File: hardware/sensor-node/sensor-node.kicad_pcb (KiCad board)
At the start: 2 copper layers, 57 x 57 mm, 52 parts, among them J1 CONUFL001-SMD-T, J2 Conn_ARM_JTAG_SWD_10, Q1 PMV250EPEA, U1 AAT1217, U2 TPS27081A, U3 SHT31-DIS, U4 24LC32, U5 MLX90614, U6 ADG633YCP, U7 TSV911RILT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

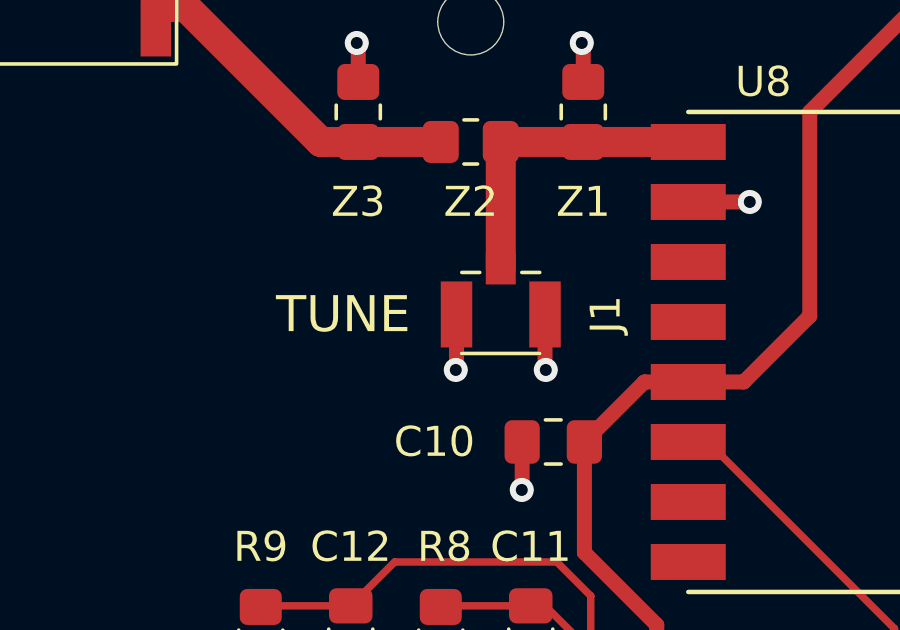
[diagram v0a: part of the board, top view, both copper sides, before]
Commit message: Add design resources and logo to PCB silkscreen
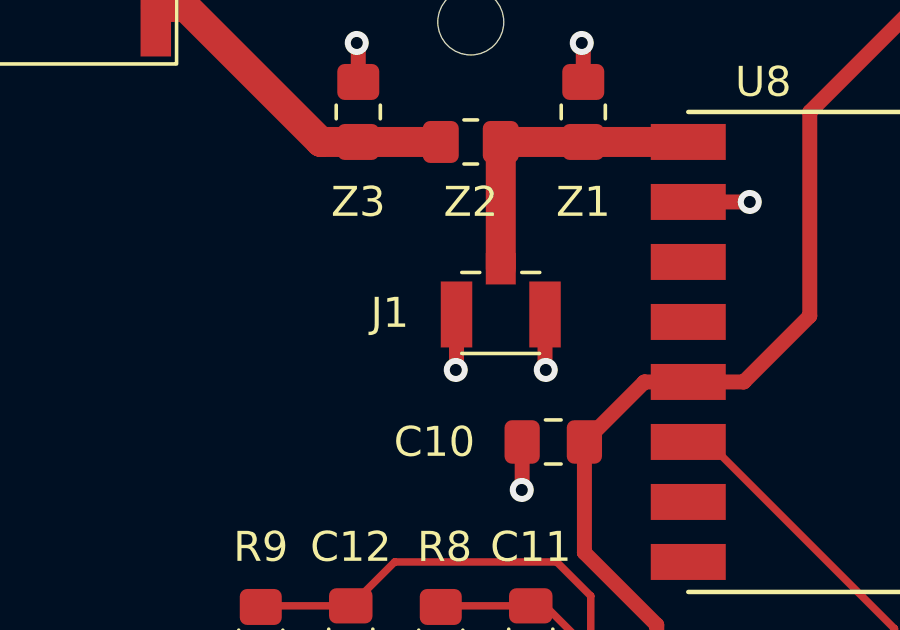
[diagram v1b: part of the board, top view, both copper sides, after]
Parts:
- added G***: LOGO, my-footprints-library:ProsperIIIKlimaMonitorLogo, B.Cu at (110.0, 46.7)
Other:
- board text added: "Sensor Node Rev. 1"
- board text removed: "FLASH"
- board text removed: "TUNE"

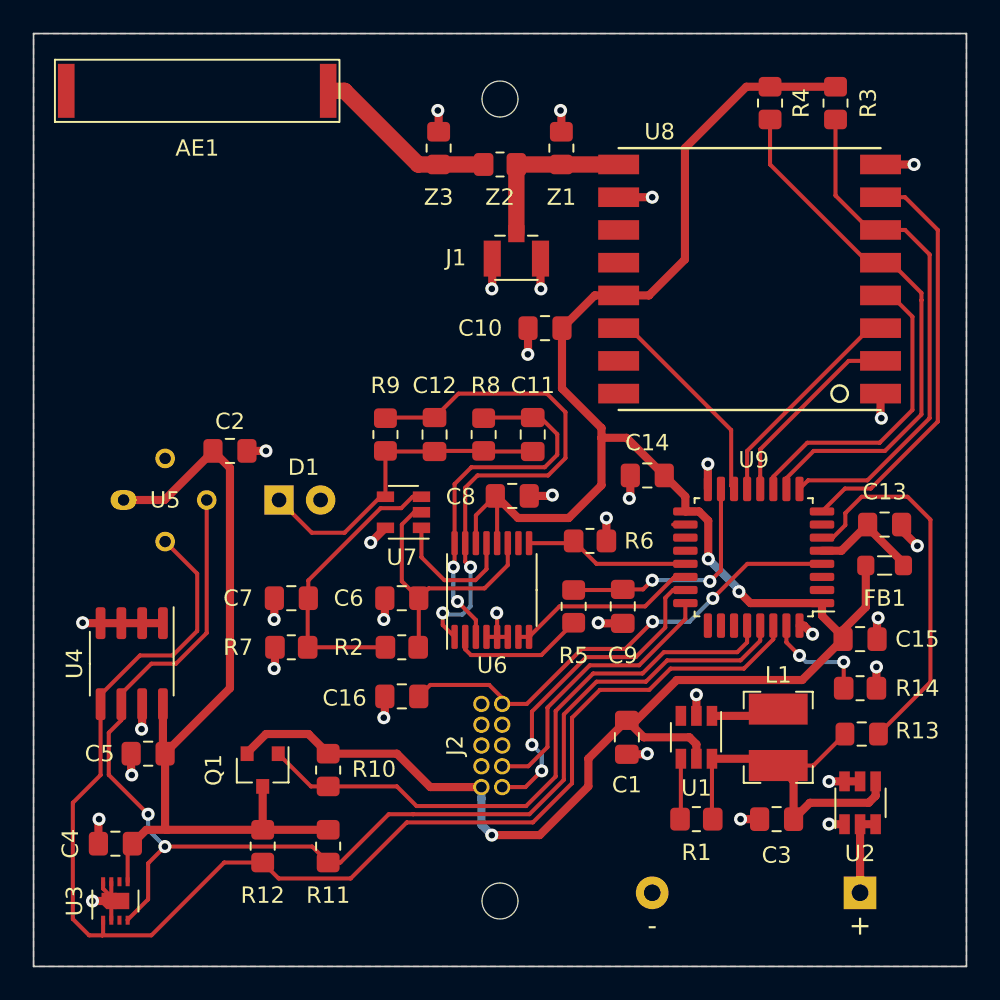
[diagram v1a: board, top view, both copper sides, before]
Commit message: Add picket fence vias
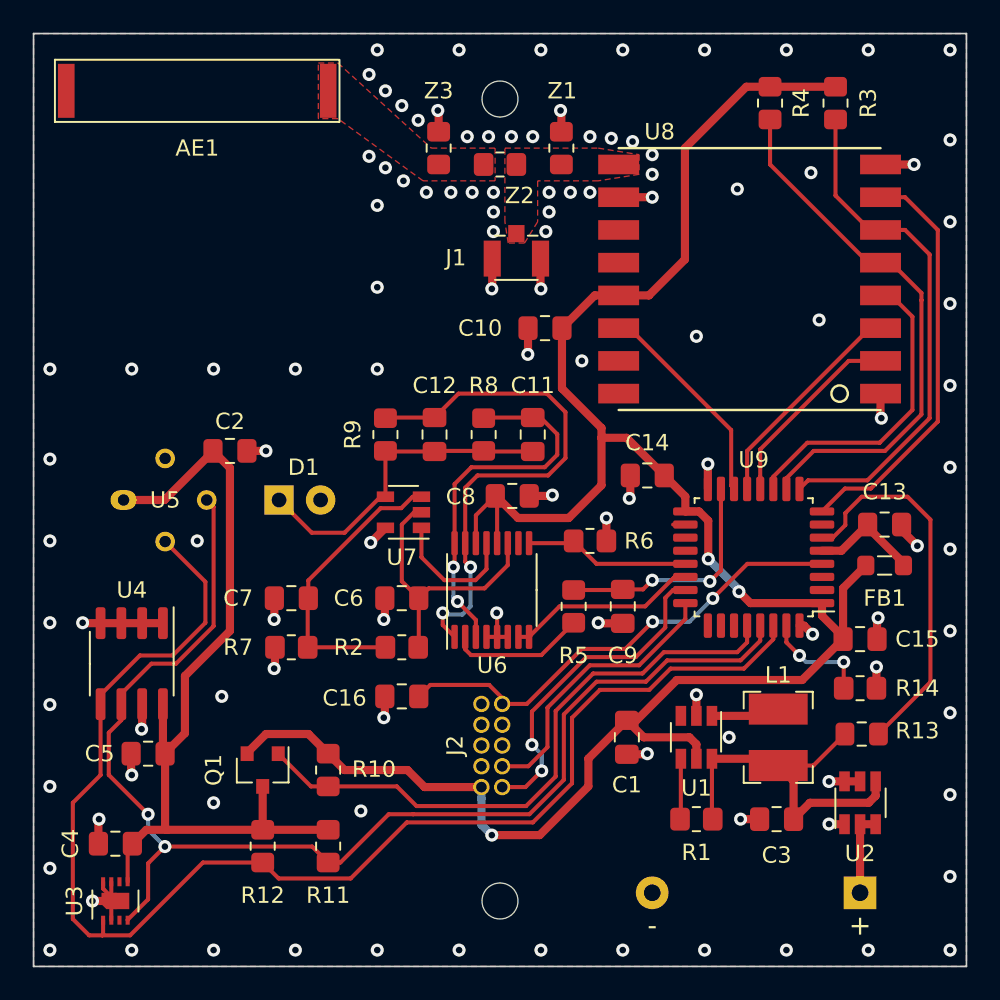
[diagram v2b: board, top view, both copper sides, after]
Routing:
- net Net-(AE1-Pad1): track 11.4 -> 0.00 mm
- net Net-(J1-Pad1): track 10.5 -> 0.00 mm
- net GND: vias 34 -> 114
- added copper zone on F.Cu, net GND
- added copper zone on F.Cu, net Net-(AE1-Pad1)
- added copper zone on F.Cu, net Net-(J1-Pad1)
- removed copper zone on F.Cu, net (none)

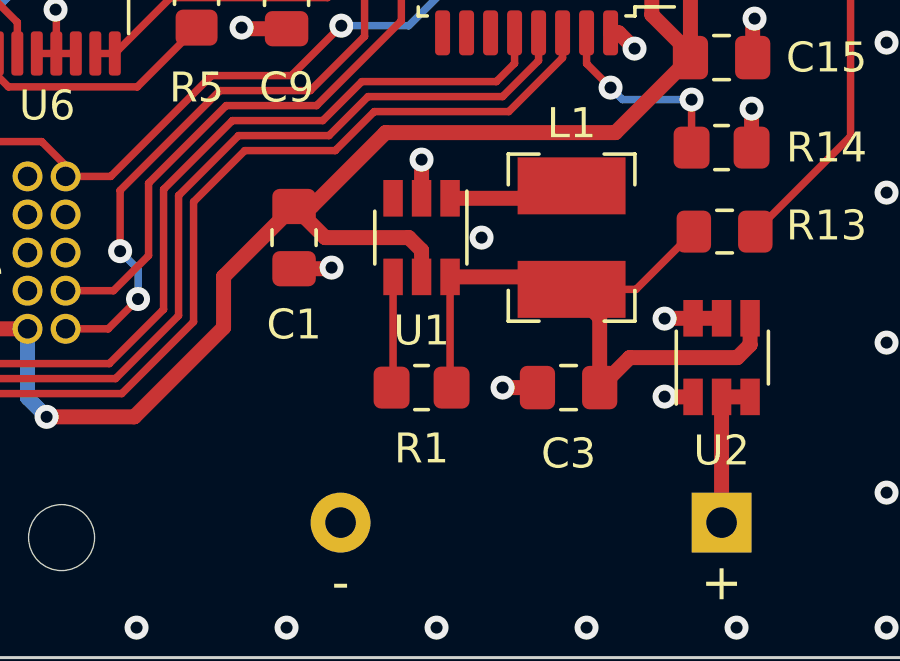
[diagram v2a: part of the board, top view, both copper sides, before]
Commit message: Switch to available boost converter
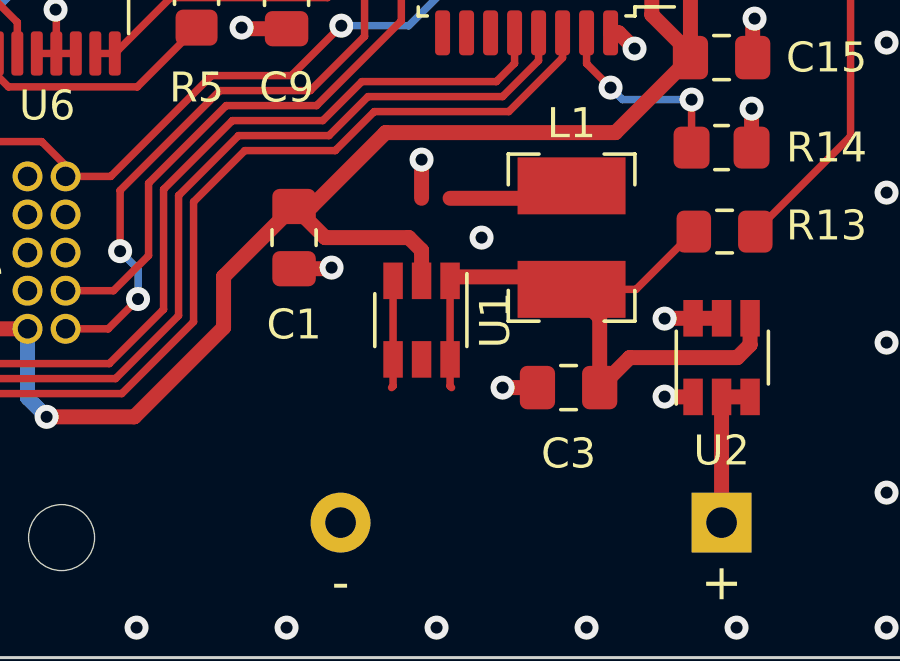
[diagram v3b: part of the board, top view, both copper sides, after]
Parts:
- removed G***: LOGO, my-footprints-library:ProsperIIIKlimaMonitorLogo
- removed R1: 1M, Resistor_SMD:R_0805_2012Metric_Pad1.20x1.40mm_HandSolder
- C1, C3: value 4.7uF -> 10uF
- U1: value AAT1217 -> TLV61225
- moved U1 2.75 mm to (140.5, 88.8)
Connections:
- U1 pad 1: Net-(L1-Pad1) -> VIN_SENSE
- U1 pad 2: GND -> +3V3
- U1 pad 3: Net-(U1-Pad3) -> GND
- U1 pad 4: Net-(R1-Pad2) -> +3V3
- U1 pad 5: +3V3 -> Net-(L1-Pad1)

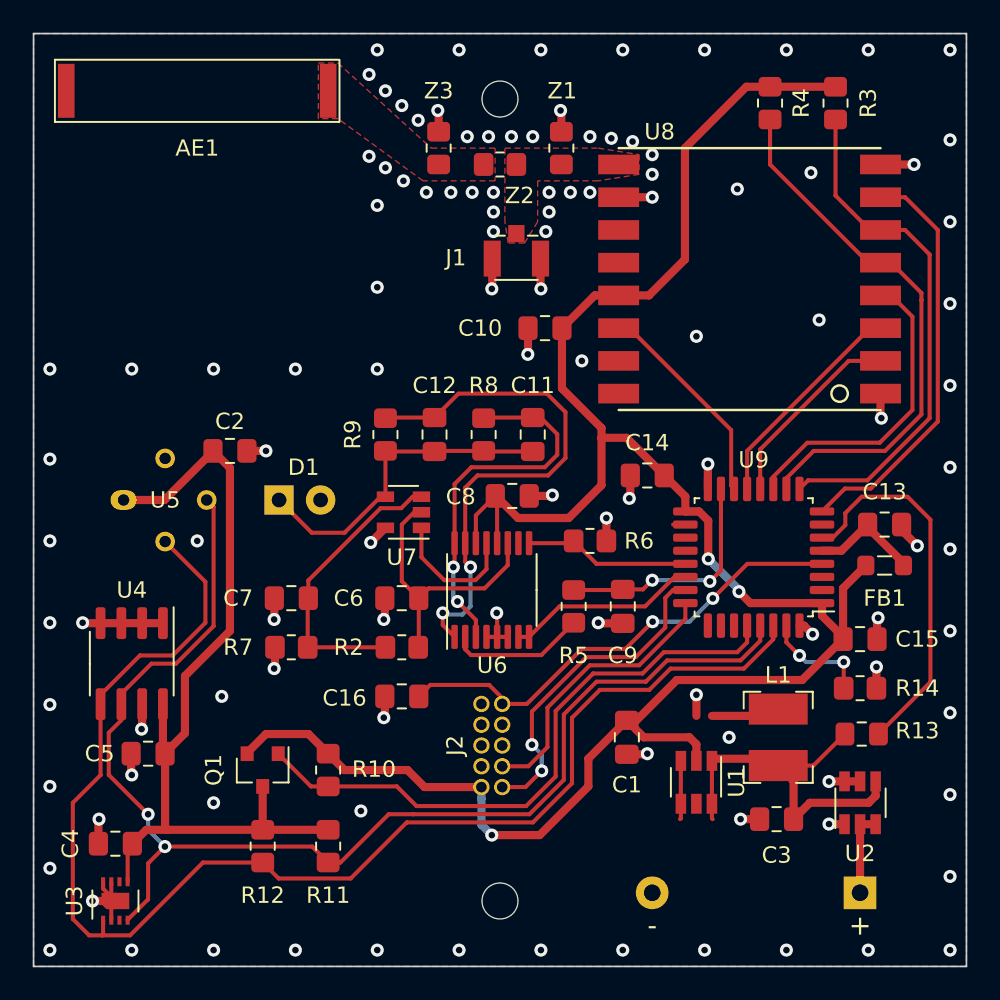
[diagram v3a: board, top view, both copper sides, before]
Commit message: Update PCB for new boost converter
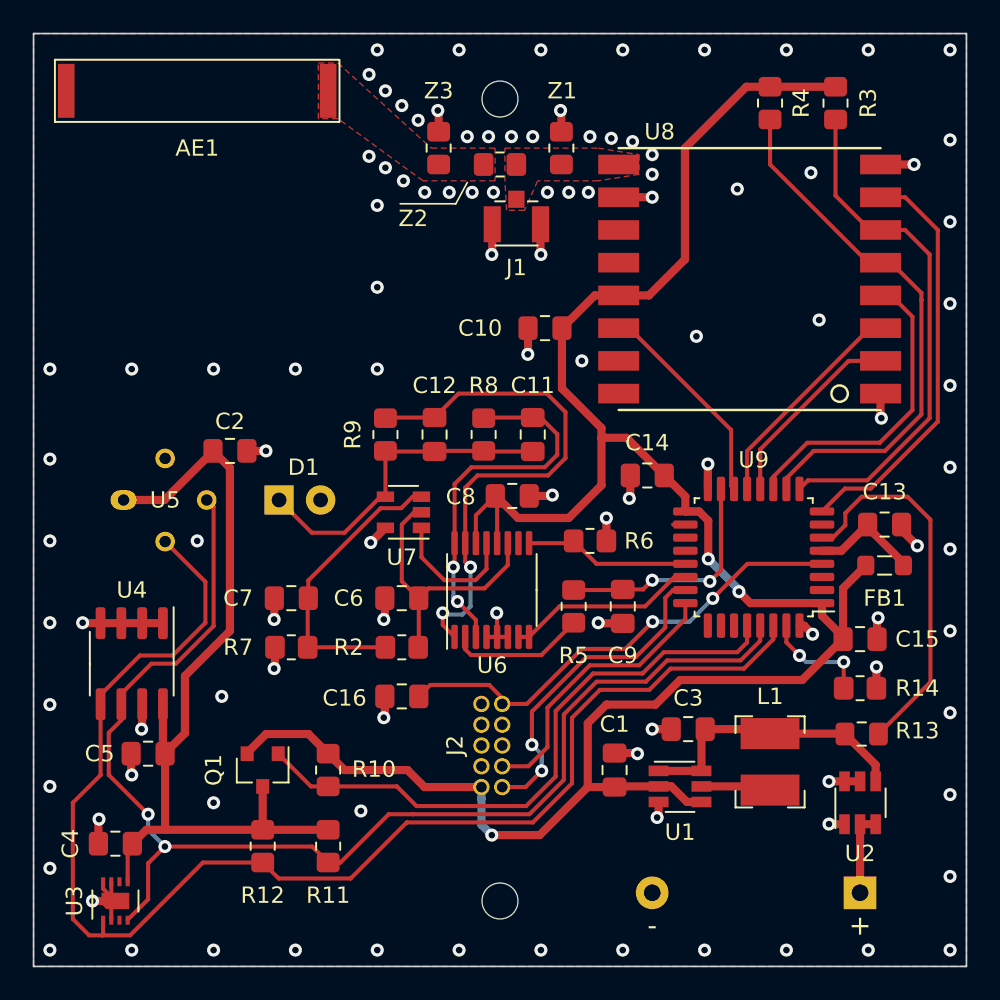
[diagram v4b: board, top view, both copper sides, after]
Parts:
- added G***: LOGO, my-footprints-library:ProsperIIIKlimaMonitorLogo, B.Cu at (110.0, 46.6)
- moved C3 7.71 mm to (140.0, 85.5)
- moved C1 2.14 mm to (135.5, 88.0), turned to 90 degrees
- moved J1 2.10 mm to (129.5, 54.6)
- moved L1 1.58 mm to (145.0, 87.5), turned to 90 degrees
- moved U1 1.03 mm to (139.5, 89.0), turned to 0 degrees
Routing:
- net VIN_SENSE: track 23.0 -> 17.6 mm
- net Net-(R1-Pad2): track 3.71 -> 0.00 mm
- net +3V3: track 131.6 -> 134.5 mm
- net GND: track 58.1 -> 57.9 mm, vias 114 -> 109

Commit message: Fix ERC & DRC errors
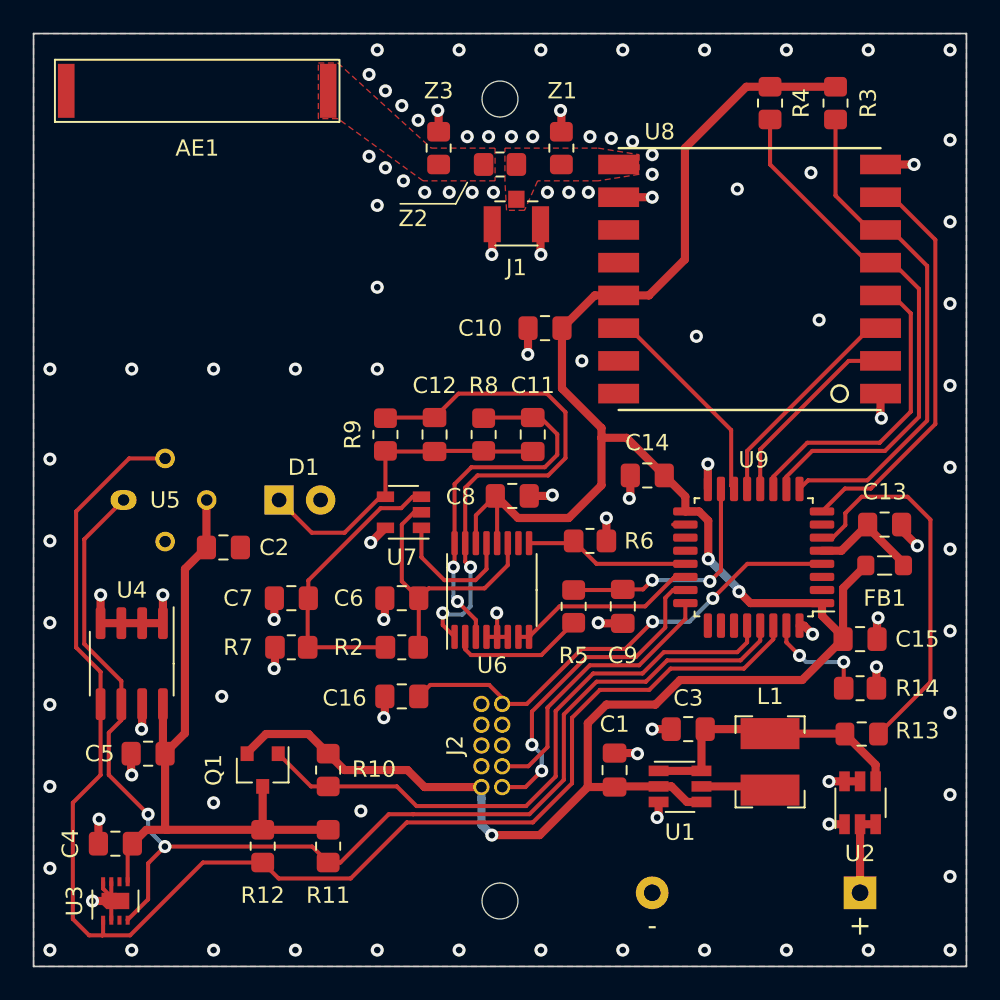
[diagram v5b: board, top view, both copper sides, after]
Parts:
- moved C2 5.91 mm to (111.6, 74.4)
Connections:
- U5 pad 1: VI2C -> SCL
- U5 pad 2: GND -> SDA
- U5 pad 3: SCL -> VI2C
- U5 pad 4: SDA -> GND
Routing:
- net VI2C: track 52.5 -> 41.7 mm
- net SDA: track 84.2 -> 89.2 mm
- net GND: track 57.9 -> 59.0 mm, vias 109 -> 108
- net SCL: track 77.4 -> 76.6 mm
- net RFM95_NRST: track 31.6 -> 31.0 mm
- net RFM95_DIO5: track 25.4 -> 24.8 mm

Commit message: Fix ADG633YRU pinout
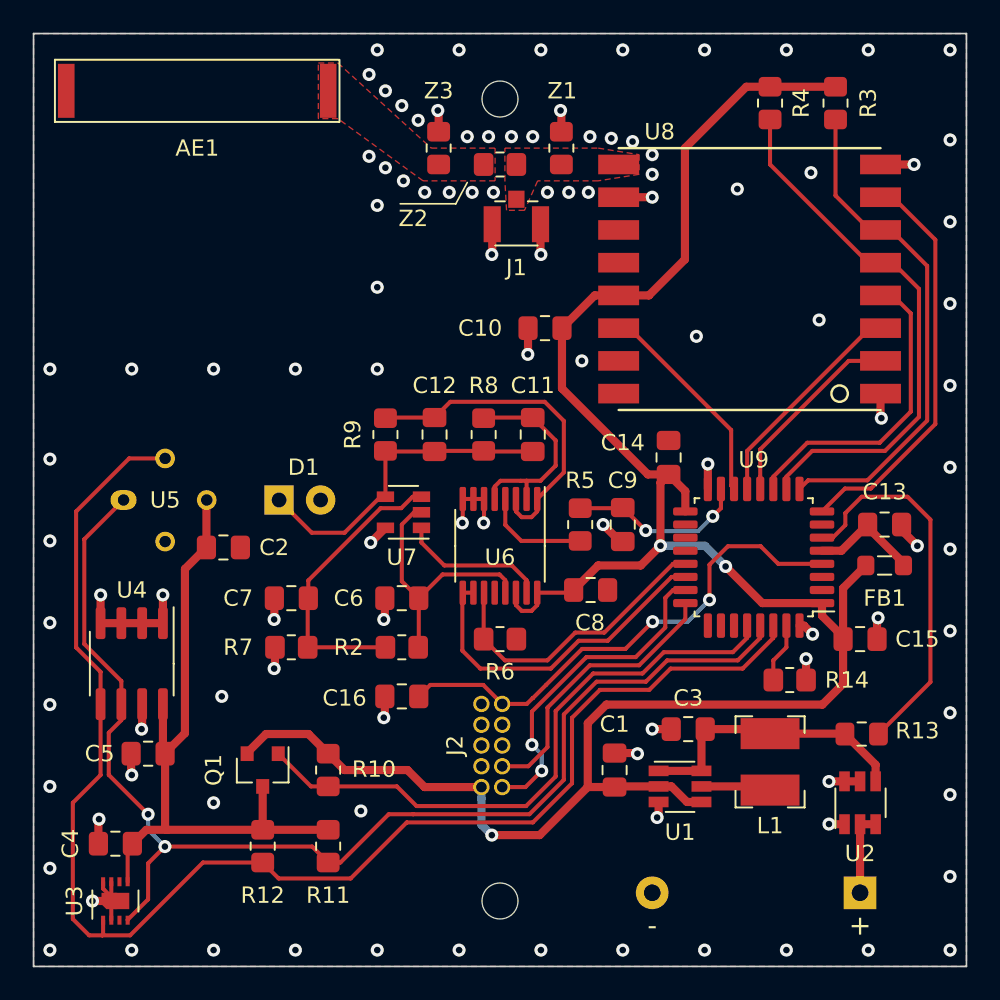
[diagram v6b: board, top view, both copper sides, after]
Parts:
- U6: value ADG633YCP -> ADG633YRU
- moved R6 8.14 mm to (128.5, 80.0)
- moved C8 7.48 mm to (134.0, 77.0)
- moved R5 5.02 mm to (133.4, 73.0)
- moved C9 5.00 mm to (136.0, 73.0)
- moved R14 4.33 mm to (146.2, 82.5)
- moved U6 2.75 mm to (128.5, 74.3), turned to 270 degrees
- moved C14 1.70 mm to (138.8, 68.9), turned to 90 degrees
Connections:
- U6 pad 10: Net-(U6-Pad10) -> PHOTO_SWITCH
- U6 pad 11: /PHOTO_VCC -> PHOTO_ENABLE
- U6 pad 12: +3V3 -> Net-(U6-Pad12)
- U6 pad 13: Net-(U6-Pad13) -> /PHOTO_VCC
- U6 pad 15: Net-(C12-Pad2) -> Net-(U6-Pad15)
- U6 pad 16: Net-(C11-Pad2) -> +3V3
- U6 pad 2: Net-(R5-Pad2) -> Net-(C11-Pad2)
- U6 pad 3: Net-(C11-Pad2) -> Net-(C12-Pad2)
- U6 pad 4: GND -> Net-(R5-Pad2)
- U6 pad 5: GND -> Net-(C11-Pad2)
- U6 pad 7: PHOTO_SWITCH -> GND
- U6 pad 8: PHOTO_SWITCH -> GND
- U6 pad 9: PHOTO_ENABLE -> PHOTO_SWITCH
- U7 pad 1: Net-(U6-Pad13) -> Net-(U6-Pad15)
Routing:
- net Net-(C12-Pad2): track 32.9 -> 20.4 mm, vias 2 -> 0
- net Net-(C11-Pad2): track 23.2 -> 12.7 mm, vias 2 -> 0
- net Net-(U6-Pad15): track 0.00 -> 9.04 mm
- net Net-(U6-Pad13): track 8.22 -> 0.00 mm
- net PHOTO_SWITCH: track 11.9 -> 20.1 mm
- net PHOTO_ENABLE: track 10.2 -> 18.2 mm
- net PHOTO_SENSE: track 14.5 -> 11.0 mm
- net Net-(R14-Pad1): track 6.62 -> 3.66 mm, vias 2 -> 0
- net GND: track 59.0 -> 56.3 mm, vias 108 -> 106
- net NRST: track 29.2 -> 31.1 mm
- net Net-(R5-Pad2): track 8.35 -> 6.57 mm
- net /PHOTO_VCC: track 17.1 -> 16.2 mm
- net Net-(U9-Pad18): track 0.75 -> 0.00 mm
